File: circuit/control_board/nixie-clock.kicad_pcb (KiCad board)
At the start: 2 copper layers, 102.7 x 51.6 mm, 46 parts, among them IC1 ATMEGA328-P, P1 CONN_2, P10 CONN_2, P2 CONN_2, P3 CONN_4, P4 CONN_4, P5 CONN_8, P6 CONN_12, P7 CONN_2, P8 CONN_2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

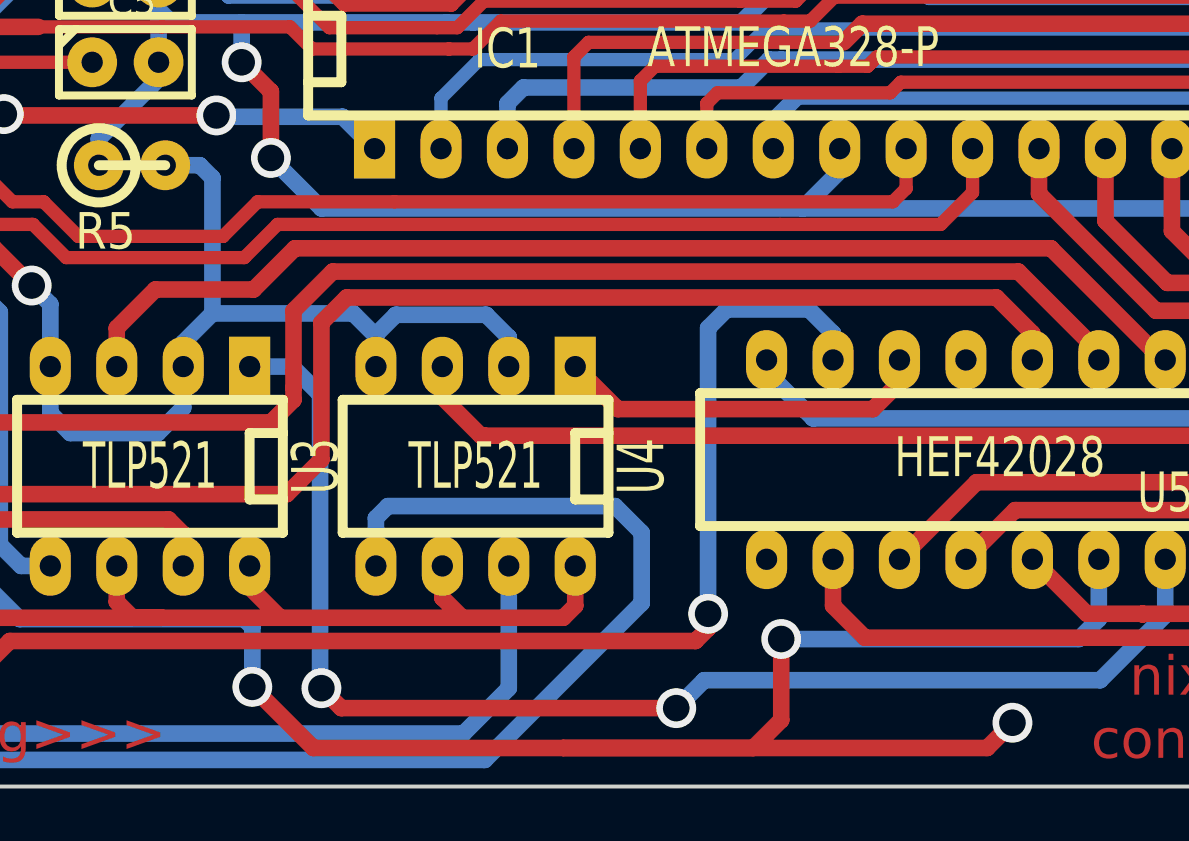
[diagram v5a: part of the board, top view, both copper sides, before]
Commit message: Control board: Remove the useless wire
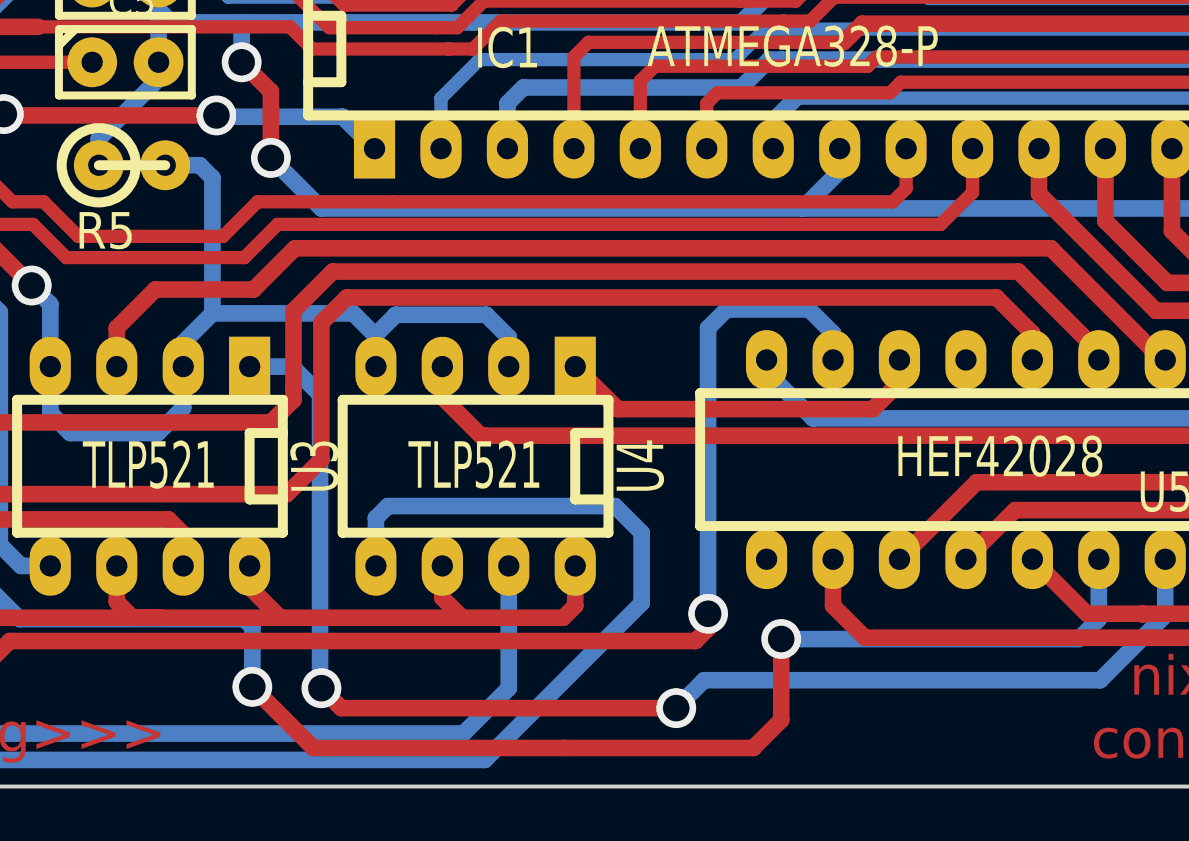
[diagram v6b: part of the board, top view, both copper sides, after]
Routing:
- net Net-(U2-Pad1): track 95.4 -> 77.5 mm, vias 3 -> 2

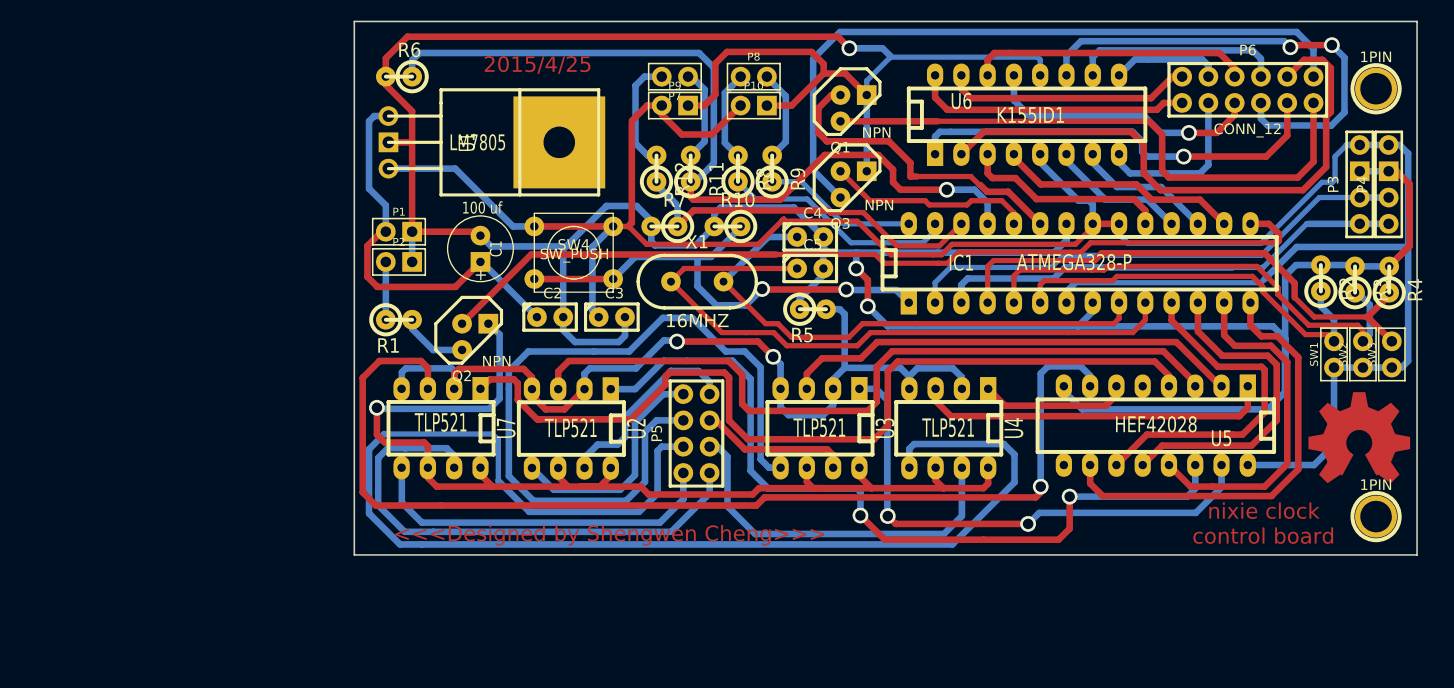
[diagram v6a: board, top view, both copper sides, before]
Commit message: Control board: Adjust the size of via drill
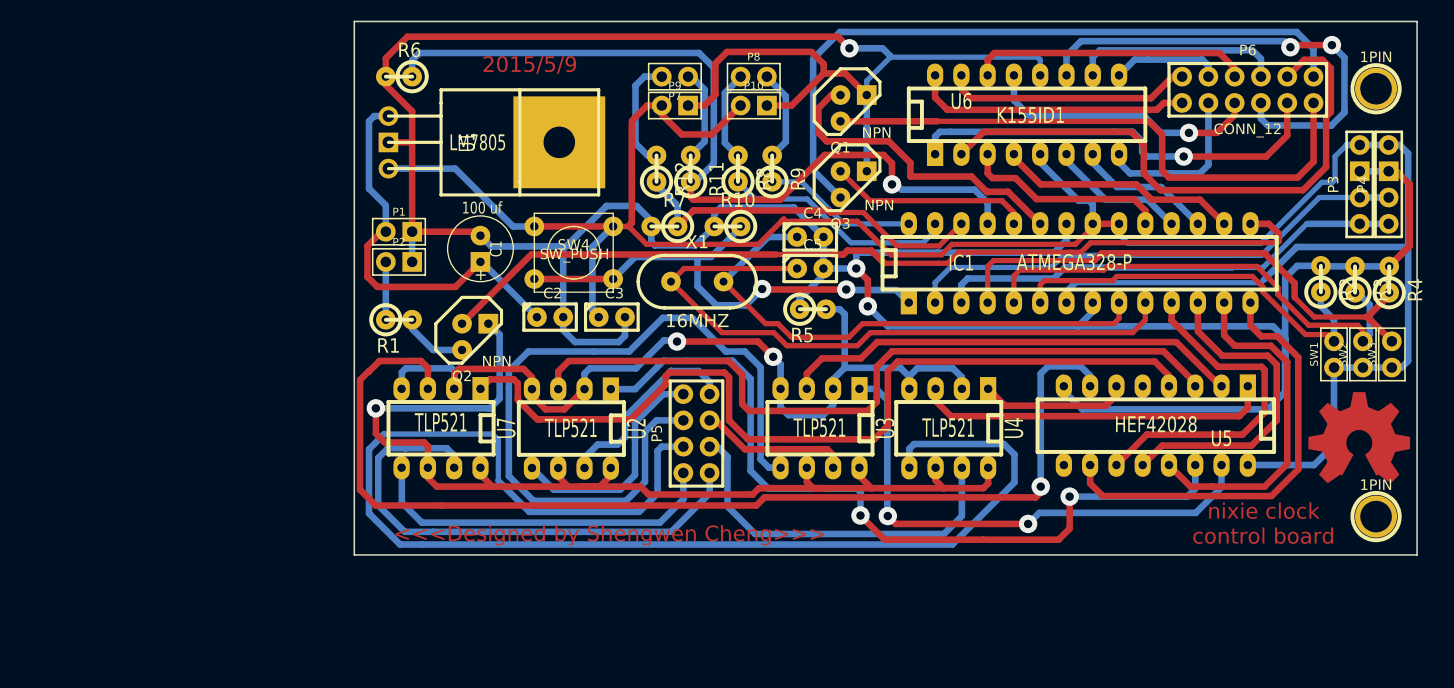
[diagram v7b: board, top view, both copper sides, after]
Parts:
- moved R2 0.08 mm to (192.2, 103.6)
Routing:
- net Left dot: track 24.6 -> 22.2 mm
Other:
- board text added: "2015/5/9"
- board text removed: "2015/4/25"
